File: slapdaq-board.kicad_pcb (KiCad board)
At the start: 0 parts

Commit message: Prepare PCB
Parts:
- added C1: 100u, Capacitor_Tantalum_SMD:CP_EIA-7260-38_AVX-R_HandSolder, F.Cu at (126.5, 100.1)
- added C10: 1n, Capacitor_SMD:C_1206_3216Metric_Pad1.33x1.80mm_HandSolder, F.Cu at (150.8, 97.7)
- added C11: 1n, Capacitor_SMD:C_1206_3216Metric_Pad1.33x1.80mm_HandSolder, F.Cu at (150.8, 101.1)
- added C12: 1n, Capacitor_SMD:C_1206_3216Metric_Pad1.33x1.80mm_HandSolder, F.Cu at (150.8, 104.4)
- added C13: 1n, Capacitor_SMD:C_1206_3216Metric_Pad1.33x1.80mm_HandSolder, F.Cu at (150.8, 107.8)
- added C14: 1n, Capacitor_SMD:C_1206_3216Metric_Pad1.33x1.80mm_HandSolder, F.Cu at (150.8, 111.1)
- added C15: 1n, Capacitor_SMD:C_1206_3216Metric_Pad1.33x1.80mm_HandSolder, F.Cu at (150.8, 114.5)
- added C16: 0.01u, Capacitor_SMD:C_1206_3216Metric_Pad1.33x1.80mm_HandSolder, F.Cu at (156.8, 97.7)
- added C17: 1u, Capacitor_SMD:C_1206_3216Metric_Pad1.33x1.80mm_HandSolder, F.Cu at (156.8, 101.1)
- added C18: 1u, Capacitor_SMD:C_1206_3216Metric_Pad1.33x1.80mm_HandSolder, F.Cu at (156.8, 104.4)
- added C19: 0.1u, Capacitor_SMD:C_1206_3216Metric_Pad1.33x1.80mm_HandSolder, F.Cu at (156.8, 107.8)
- added C2: 100u, Capacitor_Tantalum_SMD:CP_EIA-7260-38_AVX-R_HandSolder, F.Cu at (126.5, 108.1)
- added C20: 10u, Capacitor_SMD:C_1206_3216Metric_Pad1.33x1.80mm_HandSolder, F.Cu at (156.8, 111.1)
- added C21: 0.1u, Capacitor_SMD:C_1206_3216Metric_Pad1.33x1.80mm_HandSolder, F.Cu at (156.8, 114.5)
- added C22: 4.7n, Capacitor_SMD:C_1206_3216Metric_Pad1.33x1.80mm_HandSolder, F.Cu at (162.8, 97.7)
- added C23: 1u, Capacitor_SMD:C_1206_3216Metric_Pad1.33x1.80mm_HandSolder, F.Cu at (162.8, 101.1)
- added C24: 1u, Capacitor_SMD:C_1206_3216Metric_Pad1.33x1.80mm_HandSolder, F.Cu at (162.8, 104.4)
- added C25: 10u, Capacitor_SMD:C_1206_3216Metric_Pad1.33x1.80mm_HandSolder, F.Cu at (162.8, 107.8)
- added C26: 0.01u, Capacitor_SMD:C_1206_3216Metric_Pad1.33x1.80mm_HandSolder, F.Cu at (156.8, 69.0)
- added C27: 0.01u, Capacitor_SMD:C_1206_3216Metric_Pad1.33x1.80mm_HandSolder, F.Cu at (156.8, 72.4)
- added C28: 0.1u, Capacitor_SMD:C_1206_3216Metric_Pad1.33x1.80mm_HandSolder, F.Cu at (156.8, 75.7)
- added C29: 0.1u, Capacitor_SMD:C_1206_3216Metric_Pad1.33x1.80mm_HandSolder, F.Cu at (156.8, 79.1)
- added C3: 0.01u, Capacitor_SMD:C_1206_3216Metric_Pad1.33x1.80mm_HandSolder, F.Cu at (117.4, 121.8)
- added C30: 0.1u, Capacitor_SMD:C_1206_3216Metric_Pad1.33x1.80mm_HandSolder, F.Cu at (156.8, 82.4)
- added C4: 0.01u, Capacitor_SMD:C_1206_3216Metric_Pad1.33x1.80mm_HandSolder, F.Cu at (117.4, 125.2)
- added C5: 68u, Capacitor_Tantalum_SMD:CP_EIA-7132-28_AVX-C_HandSolder, F.Cu at (134.9, 114.7)
- added C6: 100u, Capacitor_Tantalum_SMD:CP_EIA-7132-28_AVX-C_HandSolder, F.Cu at (134.9, 119.9)
- added C7: 1u, Capacitor_SMD:C_1206_3216Metric_Pad1.33x1.80mm_HandSolder, F.Cu at (136.7, 83.3)
- added C8: 22u, Capacitor_SMD:C_1206_3216Metric_Pad1.33x1.80mm_HandSolder, F.Cu at (136.7, 86.6)
- added C9: 0.1u, Capacitor_SMD:C_1206_3216Metric_Pad1.33x1.80mm_HandSolder, F.Cu at (136.7, 90.0)
- added D1: BAT60A, Diode_SMD:D_SOD-323, F.Cu at (133.7, 107.5)
- added D2: BAT60A, Diode_SMD:D_SOD-323, F.Cu at (133.7, 110.4)
- added D3: D_Schottky, Diode_SMD:D_SMA_Handsoldering, F.Cu at (109.4, 122.4)
- added D4: D_Schottky, Diode_SMD:D_SMA_Handsoldering, F.Cu at (109.4, 127.0)
- added D5: POWER_LED, LED_THT:LED_D5.0mm_Horizontal_O1.27mm_Z3.0mm, F.Cu at (106.8, 83.3)
- added D6: WIFI_LED, LED_THT:LED_D5.0mm_Horizontal_O1.27mm_Z3.0mm, F.Cu at (114.3, 83.3)
- added F1: 1.5A SLOW-BLOW, Fuse:Fuse_1206_3216Metric_Pad1.42x1.75mm_HandSolder, F.Cu at (134.5, 97.7)
- added J3: USB-C, Connector_USB:USB_C_Receptacle_GCT_USB4110, F.Cu at (126.5, 86.9)
- added L1: 47u, Inductor_SMD:L_Fastron_PISN_Handsoldering, F.Cu at (112.8, 102.1)
- added L2: 68u, Inductor_SMD:L_Fastron_PISN_Handsoldering, F.Cu at (112.8, 114.1)
- added Q1: BSS84, Package_TO_SOT_SMD:SOT-23, F.Cu at (132.3, 124.7)
- added R1: 10k, Resistor_SMD:R_1206_3216Metric_Pad1.30x1.75mm_HandSolder, F.Cu at (134.5, 101.0)
- added R10: 100R, Resistor_SMD:R_1206_3216Metric_Pad1.30x1.75mm_HandSolder, F.Cu at (144.8, 104.3)
- added R11: 100R, Resistor_SMD:R_1206_3216Metric_Pad1.30x1.75mm_HandSolder, F.Cu at (144.8, 107.6)
- added R12: 100R, Resistor_SMD:R_1206_3216Metric_Pad1.30x1.75mm_HandSolder, F.Cu at (144.8, 111.0)
- added R13: 100R, Resistor_SMD:R_1206_3216Metric_Pad1.30x1.75mm_HandSolder, F.Cu at (144.8, 114.3)
- added R14: 1R, Resistor_SMD:R_1206_3216Metric_Pad1.30x1.75mm_HandSolder, F.Cu at (144.8, 117.6)
- added R15: 1R, Resistor_SMD:R_1206_3216Metric_Pad1.30x1.75mm_HandSolder, F.Cu at (144.8, 120.9)
- added R16: 100R, Resistor_SMD:R_1206_3216Metric_Pad1.30x1.75mm_HandSolder, F.Cu at (144.8, 124.2)
- added R17: 100R, Resistor_SMD:R_1206_3216Metric_Pad1.30x1.75mm_HandSolder, F.Cu at (144.8, 127.5)
- added R18: 100R, Resistor_SMD:R_1206_3216Metric_Pad1.30x1.75mm_HandSolder, F.Cu at (162.7, 75.7)
- added R19: 100R, Resistor_SMD:R_1206_3216Metric_Pad1.30x1.75mm_HandSolder, F.Cu at (162.7, 79.0)
- added R2: 10k, Resistor_SMD:R_1206_3216Metric_Pad1.30x1.75mm_HandSolder, F.Cu at (134.5, 104.3)
- added R3: 10k, Resistor_SMD:R_1206_3216Metric_Pad1.30x1.75mm_HandSolder, F.Cu at (148.8, 69.0)
- added R4: 100R, Resistor_SMD:R_1206_3216Metric_Pad1.30x1.75mm_HandSolder, F.Cu at (148.8, 72.3)
- added R5: 100R, Resistor_SMD:R_1206_3216Metric_Pad1.30x1.75mm_HandSolder, F.Cu at (148.8, 75.6)
- added R6: 5.1k, Resistor_SMD:R_1206_3216Metric_Pad1.30x1.75mm_HandSolder, F.Cu at (148.8, 78.9)
- added R7: 5.1k, Resistor_SMD:R_1206_3216Metric_Pad1.30x1.75mm_HandSolder, F.Cu at (148.8, 82.3)
- added R8: 100R, Resistor_SMD:R_1206_3216Metric_Pad1.30x1.75mm_HandSolder, F.Cu at (144.8, 97.7)
- added R9: 100R, Resistor_SMD:R_1206_3216Metric_Pad1.30x1.75mm_HandSolder, F.Cu at (144.8, 101.0)
- added U1: LM2675M-3.3, Package_SO:SOIC-8_3.9x4.9mm_P1.27mm, F.Cu at (125.6, 115.4)
- added U2: LM2675M-5, Package_SO:SOIC-8_3.9x4.9mm_P1.27mm, F.Cu at (125.6, 122.0)
- added U3: ESP32-S3, RF_Module:ESP32-S3-WROOM-1, F.Cu at (128.8, 67.6)
- added U4: DT1042-04SO-7, Package_TO_SOT_SMD:SOT-23-6, F.Cu at (142.3, 84.0)
- added U5: REF3333, Package_TO_SOT_SMD:SOT-23, F.Cu at (150.3, 125.7)
- added U6: ADS1261, Package_DFN_QFN:QFN-32-1EP_5x5mm_P0.5mm_EP3.45x3.45mm_ThermalVias, F.Cu at (151.9, 119.8)
- added U7: MAX31856, Package_SO:TSSOP-14_4.4x5mm_P0.65mm, F.Cu at (164.1, 70.8)
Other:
- copper layers 0 -> 4

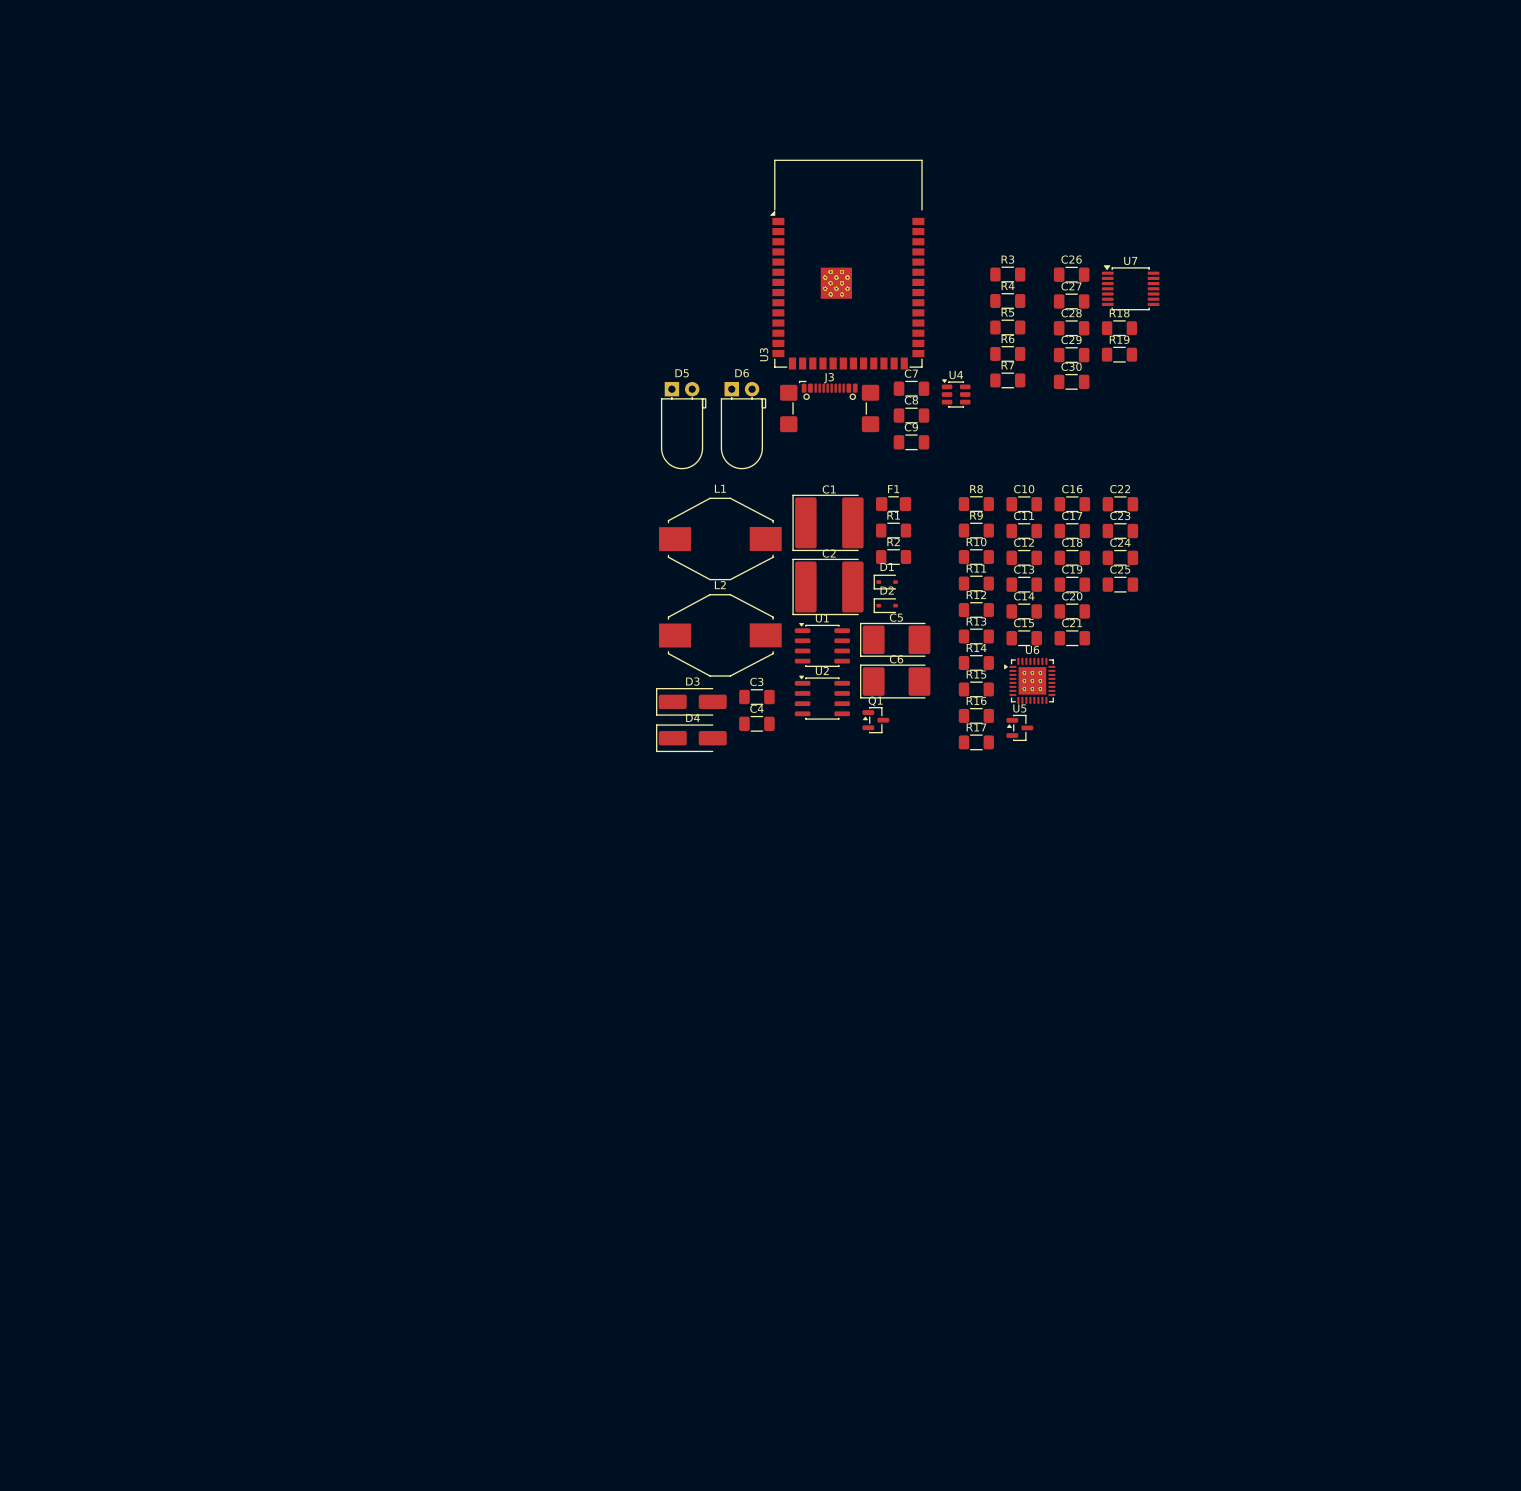
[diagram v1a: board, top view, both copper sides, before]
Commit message: started moving components around on pcb
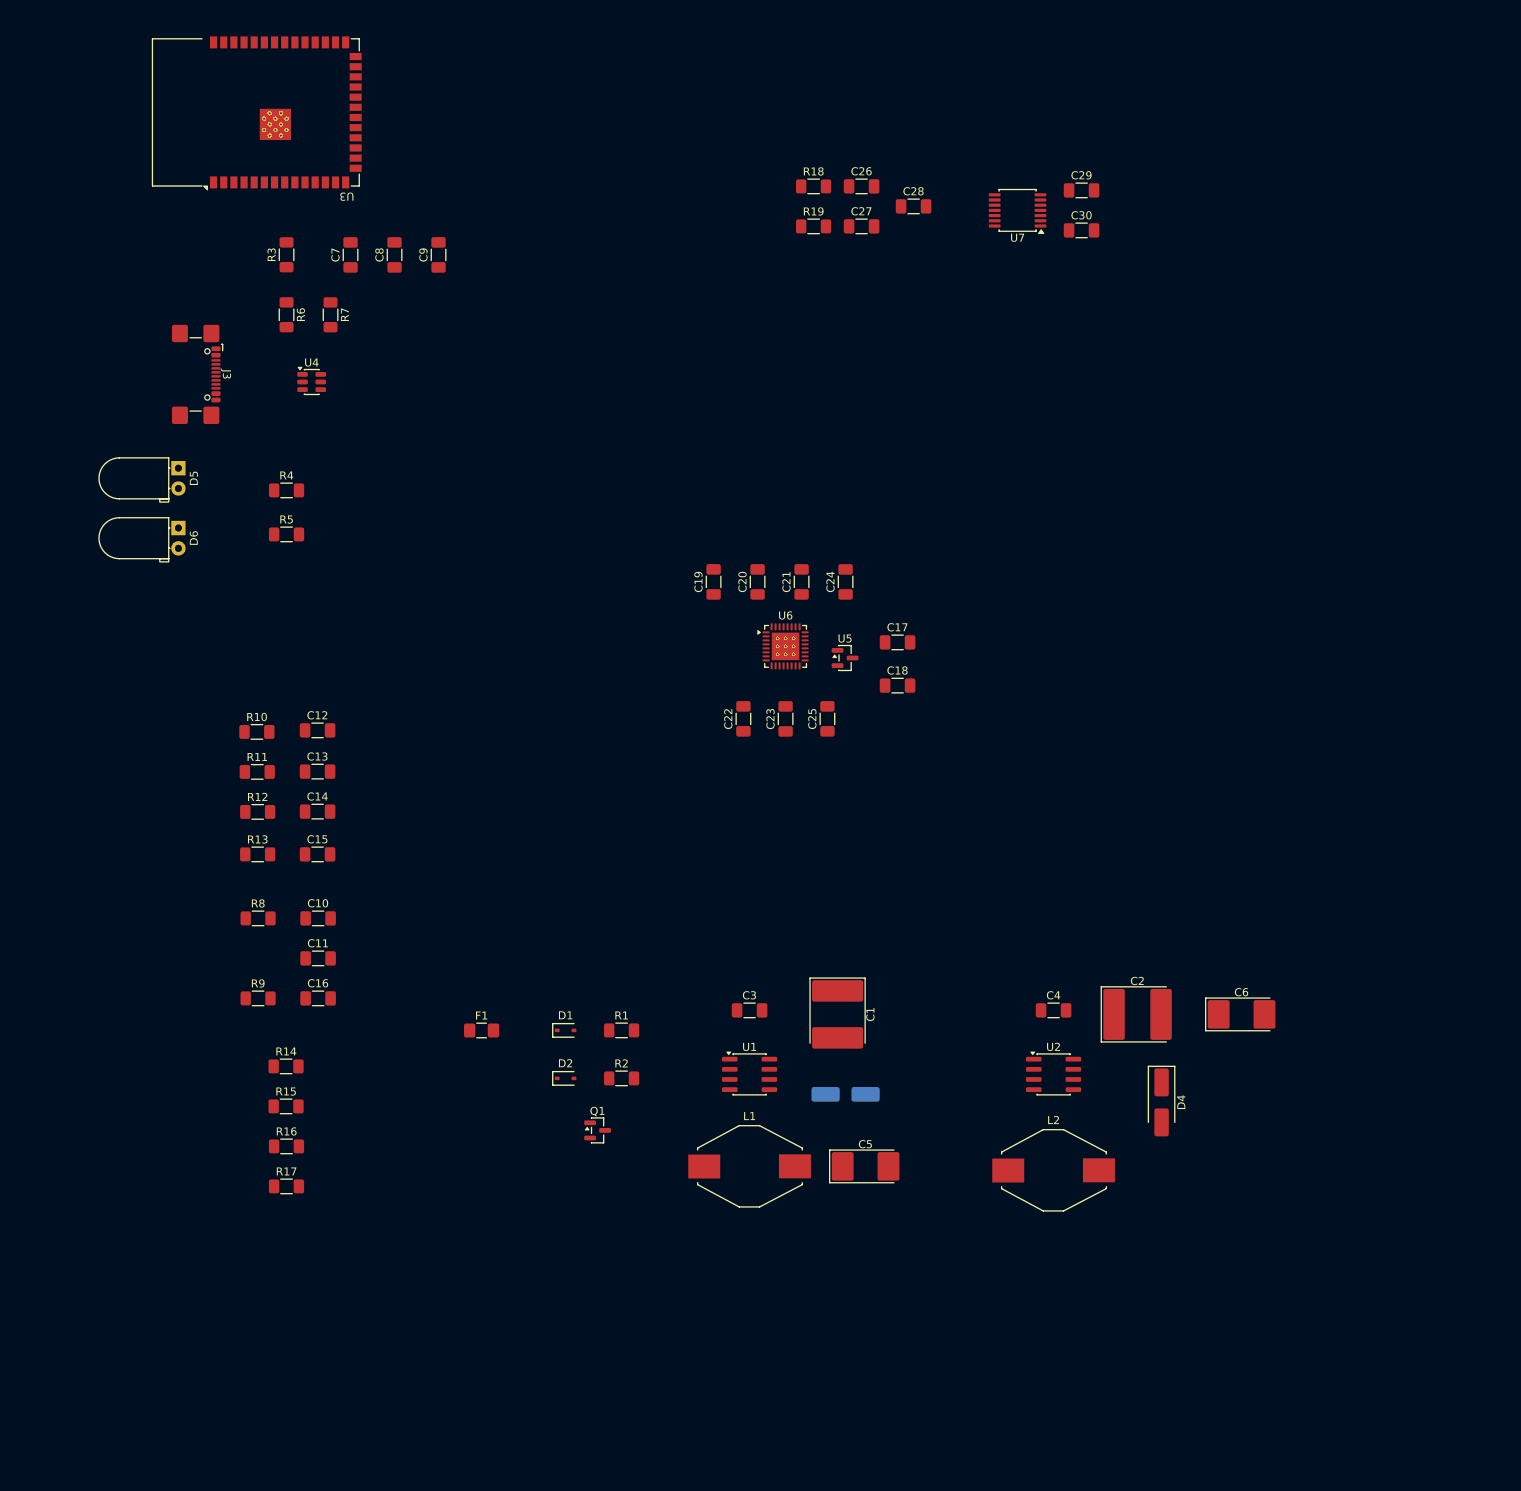
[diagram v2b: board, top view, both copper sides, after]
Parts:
- D3: moved to B.Cu
- moved C16 112.7 mm to (62.6, 159.5)
- moved R9 107.2 mm to (55.1, 159.5)
- moved R8 103.7 mm to (55.1, 149.5)
- moved C11 103.2 mm to (62.6, 154.5)
- moved R17 102.6 mm to (58.6, 183.0)
- moved C10 102.3 mm to (62.6, 149.5)
- moved R16 101.6 mm to (58.6, 178.0)
- moved R15 100.8 mm to (58.6, 173.0)
- moved R14 99.9 mm to (58.6, 168.0)
- moved R13 93.9 mm to (55.0, 141.5)
- moved R5 93.8 mm to (58.6, 101.5)
- moved R12 93.3 mm to (55.0, 136.2)
- moved R4 93.2 mm to (58.6, 96.0)
- moved R11 92.9 mm to (55.0, 131.2)
- moved R10 92.6 mm to (54.9, 126.2)
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
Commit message: pcb work
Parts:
- D3: moved to F.Cu
- moved C2 44.2 mm to (205.7, 144.5), turned to -90 degrees
- moved U2 40.9 mm to (191.8, 152.1), turned to 90 degrees
- moved D4 36.5 mm to (191.0, 144.2), turned to 0 degrees
- moved L2 35.6 mm to (175.3, 152.1), turned to 90 degrees
- moved C1 32.6 mm to (153.7, 142.0)
- moved C4 32.2 mm to (185.4, 152.1), turned to 90 degrees
- moved D3 31.5 mm to (141.6, 142.9)
- moved C5 30.8 mm to (153.7, 159.7), turned to 90 degrees
- moved U1 30.5 mm to (141.6, 151.7), turned to 90 degrees
- moved L1 29.8 mm to (124.6, 151.8), turned to 90 degrees
- moved C6 27.8 mm to (205.7, 159.7), turned to 90 degrees
- moved C3 20.3 mm to (134.6, 151.8), turned to 90 degrees
- moved R10 20.2 mm to (66.1, 109.4)
- moved R11 20.2 mm to (66.1, 114.4)
- moved C10 20.2 mm to (73.7, 132.7)
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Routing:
- net GND: track 0.00 -> 32.7 mm, vias 0 -> 2
- net Net-(U6-AIN7): track 0.00 -> 5.00 mm
- net Net-(U6-AIN2): track 0.00 -> 4.55 mm
- net Net-(U6-AIN3): track 0.00 -> 4.44 mm
- net Net-(U6-AIN4): track 0.00 -> 4.39 mm
- net Net-(U6-AIN6): track 0.00 -> 4.39 mm
- net Net-(U6-AIN5): track 0.00 -> 4.38 mm
- net Net-(U3-EN): track 0.00 -> 0.92 mm
- added copper zone on In1.Cu, net GND
- added copper zone on F.Cu, net Net-(D1-K)

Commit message: did some traces
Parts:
- moved R17 55.7 mm to (65.8, 110.7), turned to 90 degrees
- moved C12 52.6 mm to (73.2, 161.8), turned to -90 degrees
- moved R10 52.4 mm to (68.0, 161.8), turned to 90 degrees
- moved R16 50.7 mm to (71.2, 110.5), turned to 90 degrees
- moved C13 41.8 mm to (73.2, 156.2), turned to -90 degrees
- moved R11 41.8 mm to (68.0, 156.2), turned to 90 degrees
- moved R15 40.0 mm to (65.6, 116.5), turned to 90 degrees
- moved R14 34.8 mm to (71.2, 116.5), turned to 90 degrees
- moved R12 31.5 mm to (68.0, 150.8), turned to 90 degrees
- moved C14 31.2 mm to (73.2, 150.6), turned to -90 degrees
- moved C9 26.5 mm to (51.2, 68.0), turned to 180 degrees
- moved U7 24.0 mm to (114.5, 52.5)
- moved C30 22.8 mm to (124.0, 51.8)
- moved C29 22.8 mm to (124.0, 46.8)
- moved C8 21.2 mm to (51.2, 63.0), turned to 180 degrees
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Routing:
- net +3.3V: track 0.00 -> 261.8 mm
- net Net-(U6-AIN2): track 4.55 -> 80.6 mm
- net Net-(U6-AIN3): track 4.44 -> 77.9 mm
- net Net-(U6-AIN4): track 4.39 -> 72.6 mm
- net Net-(U6-AIN6): track 4.39 -> 71.8 mm
- net Net-(U6-AIN7): track 5.00 -> 72.0 mm
- net Net-(U6-AIN5): track 4.38 -> 70.4 mm
- net Net-(U6-AIN9): track 0.00 -> 61.1 mm
- net Net-(U6-AIN8): track 0.00 -> 54.3 mm
- net Net-(U7-T-): track 0.00 -> 29.4 mm
- net GND: track 32.7 -> 59.6 mm, vias 2 -> 34
- net +5V: track 0.00 -> 26.9 mm
- net Net-(U7-T+): track 0.00 -> 25.7 mm
- net Net-(U5-OUT): track 0.00 -> 18.0 mm
- net Net-(J7-Pin_2): track 0.00 -> 15.6 mm
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- added copper zone on F.Cu, net GND
- removed copper zone on In1.Cu, net GND
